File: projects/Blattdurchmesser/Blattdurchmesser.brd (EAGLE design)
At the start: 100 x 80 mm, 17 parts, among them IC1 7805TV, K1 TX2_RELAY", Q1 ARDUINOR3-NOIOREF-NOTEXT

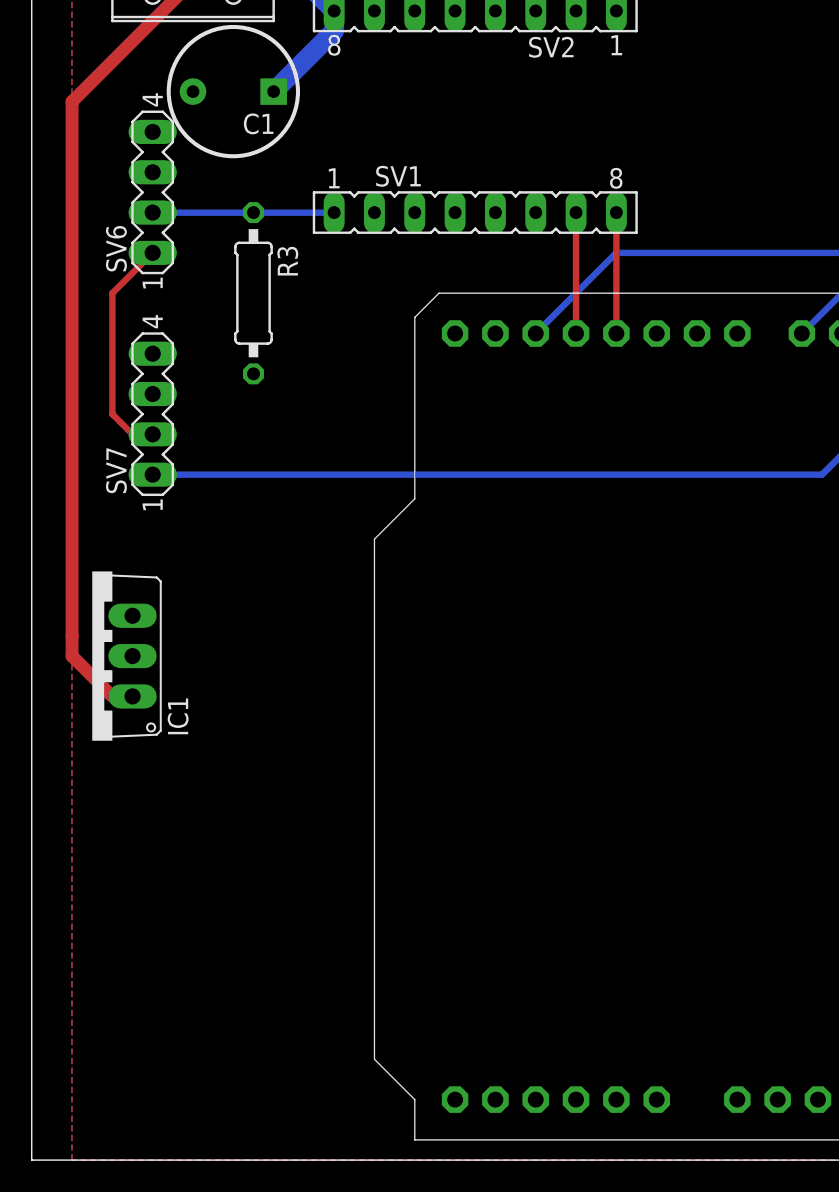
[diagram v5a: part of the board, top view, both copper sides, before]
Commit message: improvement; * replace 7805 voltage regulator by Arduino on-board one
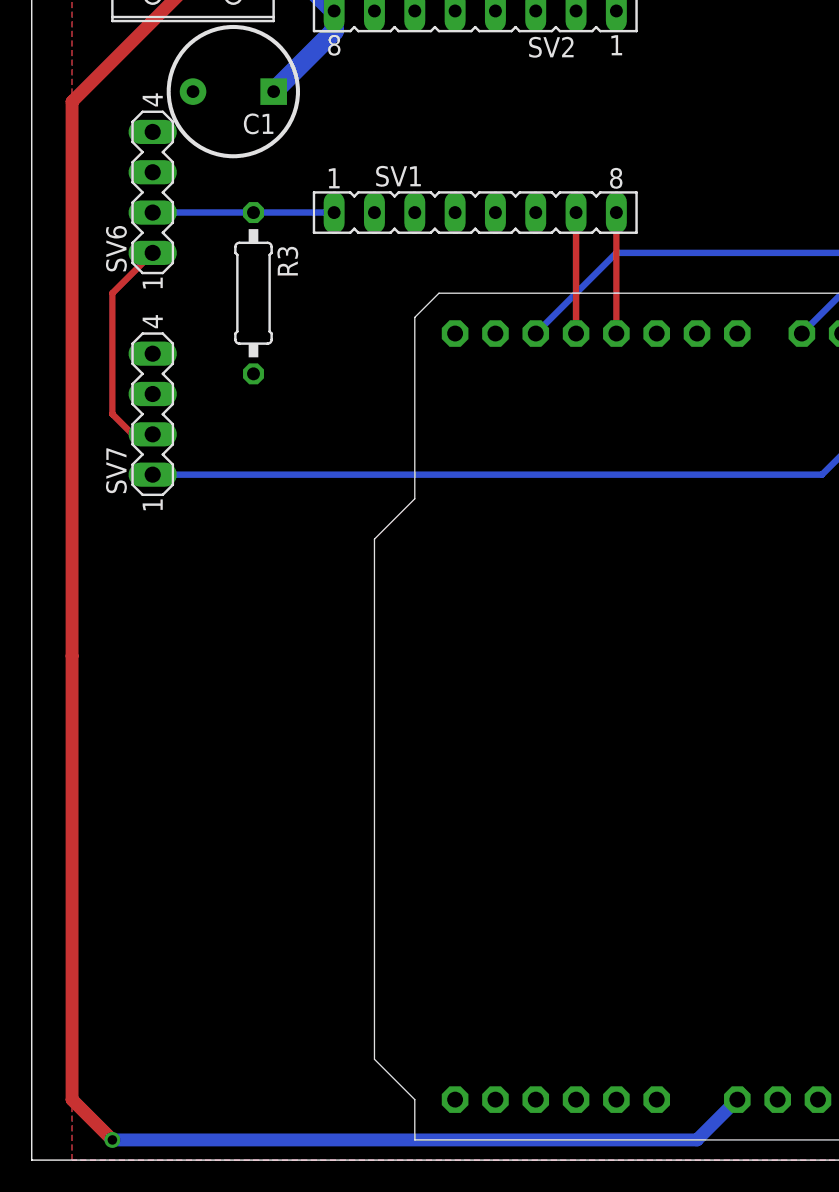
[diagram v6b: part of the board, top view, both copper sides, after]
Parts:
- removed IC1: 7805TV, linear:TO220V
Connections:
- removed net VIN: Q1.VIN
- net +12V: now also Q1.VIN; no longer IC1.1
- net +5V: no longer IC1.3
- net GND: no longer IC1.2
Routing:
- net +12V: track 69.0 -> 136.1 mm, vias 0 -> 1
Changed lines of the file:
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@@
 <attribute name="MF" value="" x="10.16" y="76.2" size="1.778" layer="27" rot="R180" display="off"/>
 </element>
-<element name="IC1" library="linear" package="TO220V" value="7805TV" x="3.81" y="31.75" rot="R90"/>
 </elements>
 <signals>
@@
 <contactref element="Q1" pad="GND"/>
 <contactref element="X1" pad="2"/>
-<contactref element="IC1" pad="2"/>
-</signal>
-<signal name="VIN">
-<contactref element="Q1" pad="VIN"/>
 </signal>
 <signal name="GND1">
@@
 <contactref element="R3" pad="2"/>
 <contactref element="Q1" pad="5V"/>
-<contactref element="IC1" pad="3"/>
 </signal>
 <signal name="+12V">
@@
 <wire x1="19.05" y1="72.39" x2="19.05" y2="71.12" width="1.2192" layer="16"/>
 <wire x1="19.05" y1="71.12" x2="15.24" y2="67.31" width="1.2192" layer="16"/>
-<contactref element="IC1" pad="1"/>
-<wire x1="2.54" y1="33.02" x2="2.54" y2="66.675" width="0.8128" layer="1"/>
+<wire x1="2.54" y1="31.75" x2="2.54" y2="66.675" width="0.8128" layer="1"/>
 <wire x1="2.54" y1="66.675" x2="12.7" y2="76.835" width="0.8128" layer="1"/>
-<wire x1="6.35" y1="29.21" x2="5.08" y2="29.21" width="0.4064" layer="1"/>
-<wire x1="5.08" y1="29.21" x2="2.54" y2="31.75" width="0.8128" layer="1"/>
-<wire x1="2.54" y1="31.75" x2="2.54" y2="33.02" width="0.8128" layer="1"/>
+<contactref element="Q1" pad="VIN"/>
+<wire x1="2.54" y1="31.75" x2="2.54" y2="3.81" width="0.8128" layer="1"/>
+<wire x1="2.54" y1="3.81" x2="5.08" y2="1.27" width="0.8128" layer="1"/>
+<via x="5.08" y="1.27" extent="1-16" drill="0.6"/>
+<wire x1="5.08" y1="1.27" x2="41.91" y2="1.27" width="0.8128" layer="16"/>
+<wire x1="41.91" y1="1.27" x2="44.45" y2="3.81" width="0.8128" layer="16"/>
 </signal>
 <signal name="N$3">
